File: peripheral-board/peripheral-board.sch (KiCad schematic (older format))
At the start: 12 parts, among them CON1001 AVR-ISP-10, P1001 Peripheral Bus, P1002 Power, SW1001 Power, U1001 ATTINY48-A

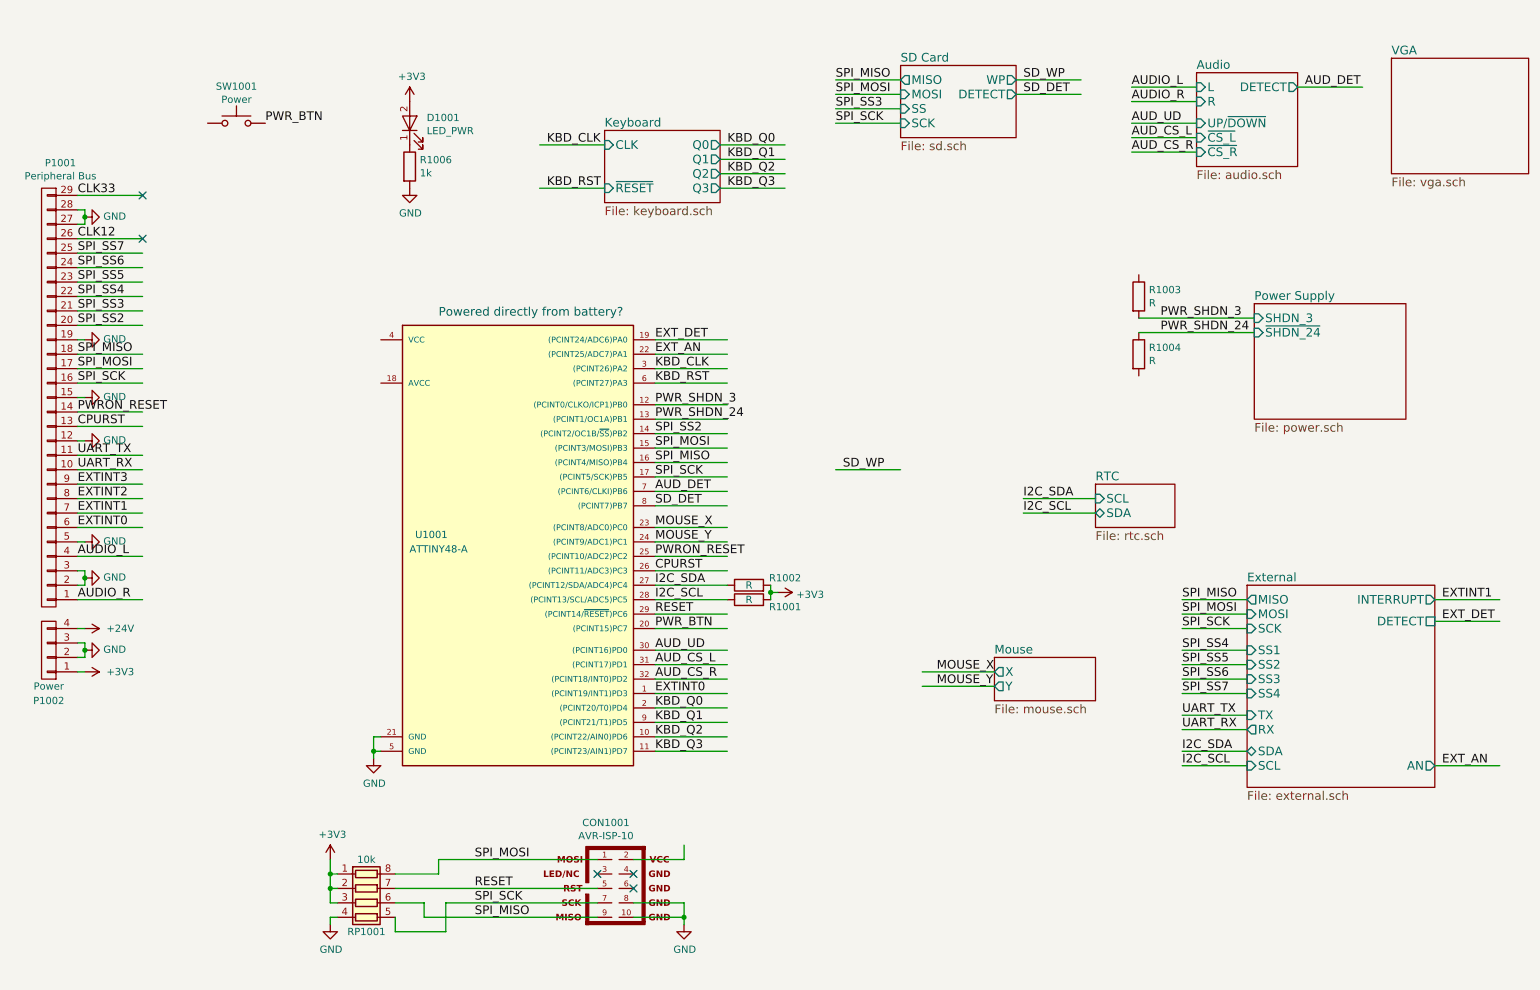
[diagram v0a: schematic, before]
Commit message: added linear 3v3 reg for keyboard micro
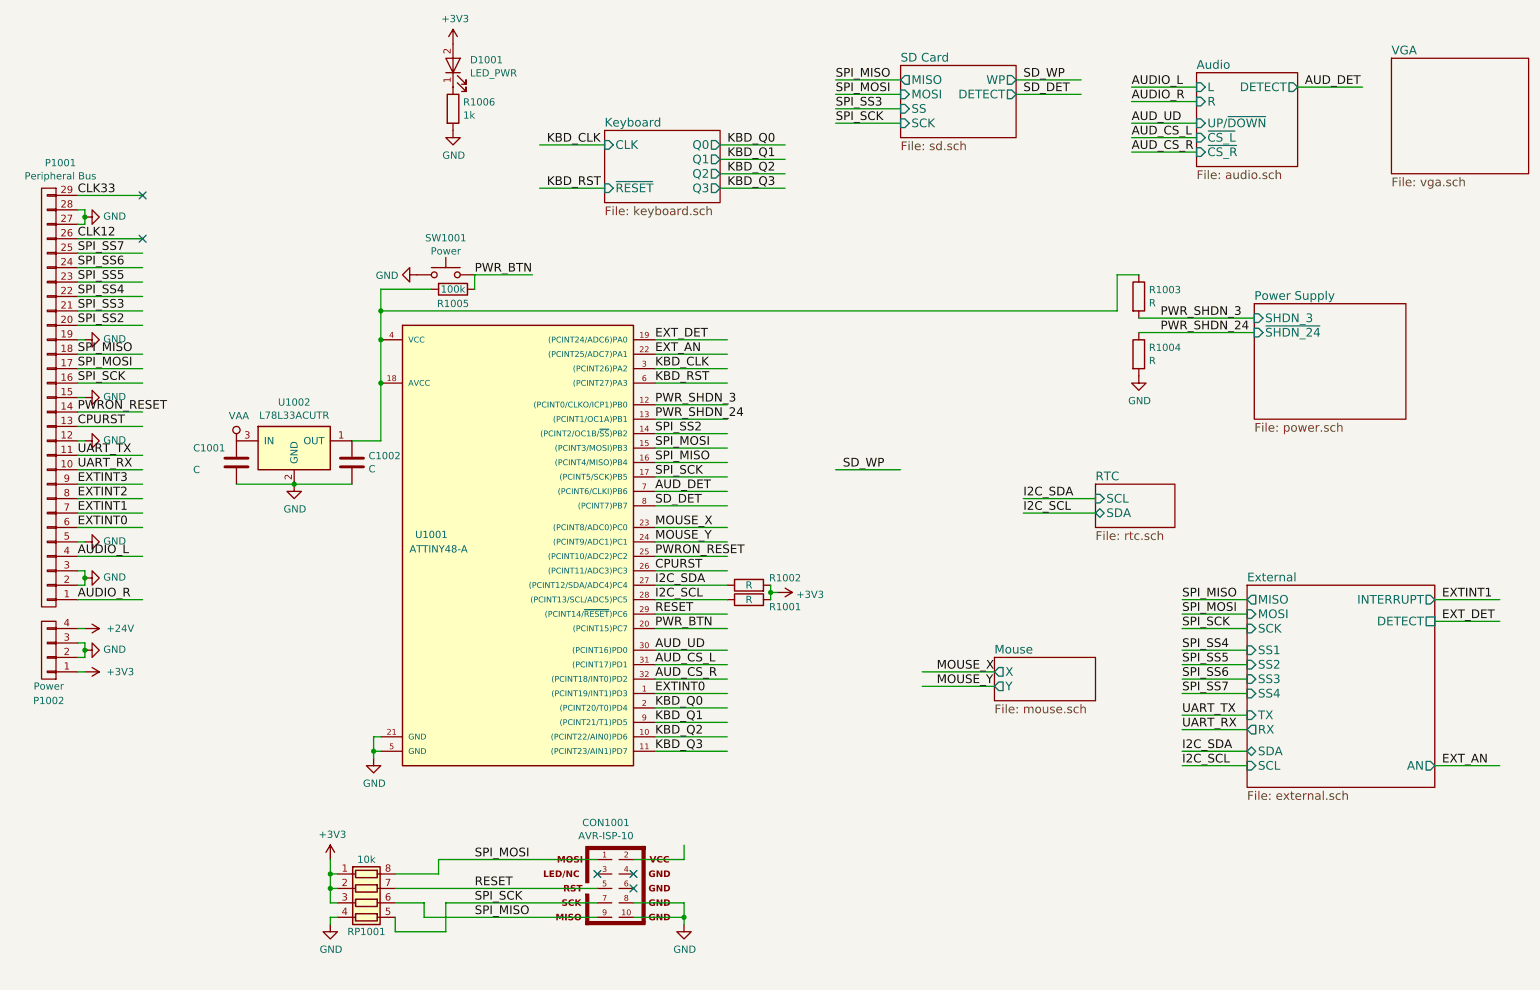
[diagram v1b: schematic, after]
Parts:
- added C1001, C1002: C, Capacitors_SMD:C_0805, symbol C
- added R1005: 100k, Resistors_SMD:R_0805, symbol R
- added U1002: L78L33ACUTR, TO_SOT_Packages_SMD:SOT89-3_Housing, symbol MC78L05ACH
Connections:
- net labels added: VAA
- wire segments 130 -> 139
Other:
- note removed: "Powered directly from battery?"
- moved on the sheet: D1001, R1006, SW1001
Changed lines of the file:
@@
 	1    0    0    -1
 $EndComp
-Text Notes 3450 2650 0    60   ~ 0
-Powered directly from battery?
 $Comp
 L CONN_01X04 P1002
@@
 L SW_Push SW1001
 U 1 1 5823964C
-P 2050 1300
-F 0 "SW1001" H 2050 1555 50  0000 C CNN
-F 1 "Power" H 2050 1464 50  0000 C CNN
-F 2 "lib:SMD-TACT-5.2x5.2x2mm" H 2050 1300 50  0001 C CNN
-F 3 "" H 2050 1300 50  0000 C CNN
-	1    2050 1300
+P 3500 2350
+F 0 "SW1001" H 3500 2605 50  0000 C CNN
+F 1 "Power" H 3500 2514 50  0000 C CNN
+F 2 "lib:SMD-TACT-5.2x5.2x2mm" H 3500 2350 50  0001 C CNN
+F 3 "" H 3500 2350 50  0000 C CNN
+	1    3500 2350
 	1    0    0    -1
 $EndComp
@@
 Text Label 4950 3100 0    60   ~ 0
 KBD_RST
-Text Label 2250 1300 0    60   ~ 0
+Text Label 3700 2350 0    60   ~ 0
 PWR_BTN
 Text Label 4950 5250 0    60   ~ 0
@@
 L LED D1001
 U 1 1 58A4D1EF
-P 3250 1300
-F 0 "D1001" V 3288 1182 50  0000 R CNN
-F 1 "LED_PWR" V 3197 1182 50  0000 R CNN
-F 2 "LEDs:LED-3MM" H -50 -750 50  0001 C CNN
-F 3 "" H -50 -750 50  0001 C CNN
-	1    3250 1300
+P 3550 900
+F 0 "D1001" V 3588 782 50  0000 R CNN
+F 1 "LED_PWR" V 3497 782 50  0000 R CNN
+F 2 "LEDs:LED-3MM" H 250 -1150 50  0001 C CNN
+F 3 "" H 250 -1150 50  0001 C CNN
+	1    3550 900
 	0    -1   -1   0
 $EndComp
@@
 L R R1006
 U 1 1 58A4D893
-P 3250 1600
-F 0 "R1006" H 3320 1646 50  0000 L CNN
-F 1 "1k" H 3320 1555 50  0000 L CNN
-F 2 "Resistors_SMD:R_0805" V -170 -400 50  0001 C CNN
-F 3 "" H -100 -400 50  0001 C CNN
-	1    3250 1600
+P 3550 1200
+F 0 "R1006" H 3620 1246 50  0000 L CNN
+F 1 "1k" H 3620 1155 50  0000 L CNN
+F 2 "Resistors_SMD:R_0805" V 130 -800 50  0001 C CNN
+F 3 "" H 200 -800 50  0001 C CNN
+	1    3550 1200
 	1    0    0    -1
 $EndComp
@@
 L GND #PWR015
 U 1 1 58A4D9DD
-P 3250 1750
-F 0 "#PWR015" H -50 -250 50  0001 C CNN
-F 1 "GND" H 3255 1577 50  0000 C CNN
-F 2 "" H -50 0   50  0001 C CNN
-F 3 "" H -50 0   50  0001 C CNN
-	1    3250 1750
+P 3550 1350
+F 0 "#PWR015" H 250 -650 50  0001 C CNN
+F 1 "GND" H 3555 1177 50  0000 C CNN
+F 2 "" H 250 -400 50  0001 C CNN
+F 3 "" H 250 -400 50  0001 C CNN
+	1    3550 1350
 	1    0    0    -1
 $EndComp
@@
 L +3V3 #PWR016
 U 1 1 58A4DB27
-P 3250 1150
-F 0 "#PWR016" H -200 -800 50  0001 C CNN
-F 1 "+3V3" H 3265 1323 50  0000 C CNN
-F 2 "" H -200 -650 50  0001 C CNN
-F 3 "" H -200 -650 50  0001 C CNN
-	1    3250 1150
-	1    0    0    -1
-$EndComp
+P 3550 750
+F 0 "#PWR016" H 100 -1200 50  0001 C CNN
+F 1 "+3V3" H 3565 923 50  0000 C CNN
+F 2 "" H 100 -1050 50  0001 C CNN
+F 3 "" H 100 -1050 50  0001 C CNN
+	1    3550 750
+	1    0    0    -1
+$EndComp
+$Comp
+L MC78L05ACH U1002
+U 1 1 58A5B00E
+P 2450 3550
+F 0 "U1002" H 2450 3867 50  0000 C CNN
+F 1 "L78L33ACUTR" H 2450 3776 50  0000 C CNN
+F 2 "TO_SOT_Packages_SMD:SOT89-3_Housing" H -50 1150 50  0001 C CNN
+F 3 "" H -50 1150 50  0001 C CNN
+	1    2450 3550
+	1    0    0    -1
+$EndComp
+$Comp
+L C C1001
+U 1 1 58A5F9BD
+P 2050 3650
+F 0 "C1001" H 1750 3750 50  0000 L CNN
+F 1 "C" H 1750 3600 50  0000 L CNN
+F 2 "Capacitors_SMD:C_0805" H -1062 1250 50  0001 C CNN
+F 3 "" H -1100 1400 50  0001 C CNN
+	1    2050 3650
+	1    0    0    -1
+$EndComp
+$Comp
+L C C1002
+U 1 1 58A5FB28
+P 2850 3650
+F 0 "C1002" H 2965 3696 50  0000 L CNN
+F 1 "C" H 2965 3605 50  0000 L CNN
+F 2 "Capacitors_SMD:C_0805" H -112 950 50  0001 C CNN
+F 3 "" H -150 1100 50  0001 C CNN
+	1    2850 3650
+	1    0    0    -1
+$EndComp
+Wire Wire Line
+	2050 3800 2850 3800
+Connection ~ 2450 3800
+$Comp
+L GND #PWR017
+U 1 1 58A610B7
+P 2450 3800
+F 0 "#PWR017" H -200 -450 50  0001 C CNN
+F 1 "GND" H 2455 3627 50  0000 C CNN
+F 2 "" H -200 -200 50  0001 C CNN
+F 3 "" H -200 -200 50  0001 C CNN
+	1    2450 3800
+	1    0    0    -1
+$EndComp
+$Comp
+L VAA #PWR018
+U 1 1 58A6141E
+P 2050 3500
+F 0 "#PWR018" H -350 200 50  0001 C CNN
+F 1 "VAA" H 2067 3673 50  0000 C CNN
+F 2 "" H -350 350 50  0001 C CNN
+F 3 "" H -350 350 50  0001 C CNN
+	1    2050 3500
+	1    0    0    -1
+$EndComp
+Wire Wire Line
+	2850 3500 3050 3500
+Connection ~ 3050 3100
+Connection ~ 3050 2800
+$Comp
+L R R1005
+U 1 1 58A61F8B
+P 3550 2450
+F 0 "R1005" V 3650 2450 50  0000 C CNN
+F 1 "100k" V 3550 2450 50  0000 C CNN
+F 2 "Resistors_SMD:R_0805" V -970 200 50  0001 C CNN
+F 3 "" H -900 200 50  0001 C CNN
+	1    3550 2450
+	0    1    1    0
+$EndComp
+Wire Wire Line
+	3700 2350 4100 2350
+Wire Wire Line
+	3700 2450 3700 2350
+$Comp
+L GND #PWR019
+U 1 1 58A62D39
+P 3300 2350
+F 0 "#PWR019" H -950 -400 50  0001 C CNN
+F 1 "GND" V 3305 2222 50  0000 R CNN
+F 2 "" H -950 -150 50  0001 C CNN
+F 3 "" H -950 -150 50  0001 C CNN
+	1    3300 2350
+	0    1    1    0
+$EndComp
+Wire Wire Line
+	3050 3500 3050 2450
+Wire Wire Line
+	3050 2450 3400 2450
+Wire Wire Line
+	3050 2600 8150 2600
+Wire Wire Line
+	8150 2600 8150 2350
+Wire Wire Line
+	8150 2350 8300 2350
+Connection ~ 3050 2600
+$Comp
+L GND #PWR020
+U 1 1 58A674BE
+P 8300 3050
+F 0 "#PWR020" H 8350 3100 50  0001 C CNN
+F 1 "GND" H 8305 2877 50  0000 C CNN
+F 2 "" H 50  -50 50  0001 C CNN
+F 3 "" H 50  -50 50  0001 C CNN
+	1    8300 3050
+	1    0    0    -1
+$EndComp

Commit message: routed traces.
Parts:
- removed CON1001: AVR-ISP-10, Connect:IDC_Header_Straight_10pins, symbol AVR-ISP-10
- removed RP1001: 10k, Resistors_SMD:R_Cat16-4, symbol R_Pack04
- added R1007: 10k, Resistors_SMD:R_0805, symbol R
- added R1008, R1009, R1010: 47k, Resistors_SMD:R_0805, symbol R
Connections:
- net labels added: +3.3VP
- wire segments 139 -> 117
- no-connect marks 5 -> 2
